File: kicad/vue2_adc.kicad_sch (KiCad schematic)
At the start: 141 parts, among them J1 AudioJack3_Ground, J10 AudioJack3_Ground, J11 AudioJack3_Ground, J12 AudioJack3_Ground, J13 AudioJack3_Ground, J14 AudioJack3_Ground, J15 AudioJack3_Ground, J16 AudioJack3_Ground, J18 AudioJack3_Ground, J19 AudioJack3_Ground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

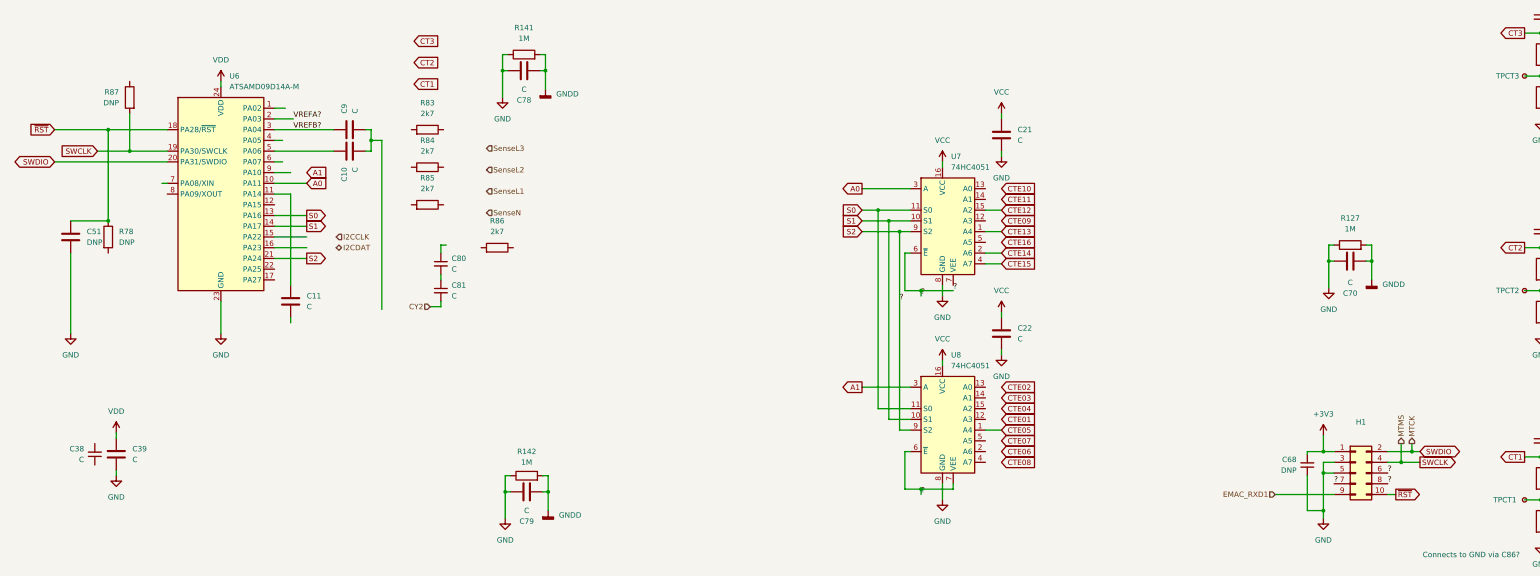
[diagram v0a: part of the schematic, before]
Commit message: Update schematic
As described in https://github.com/emporia-vue-local/esphome/discussions/173#discussioncomment-6137086

Thank you @g3gg0!

Also this ends up upgrading the project to Kicad 7
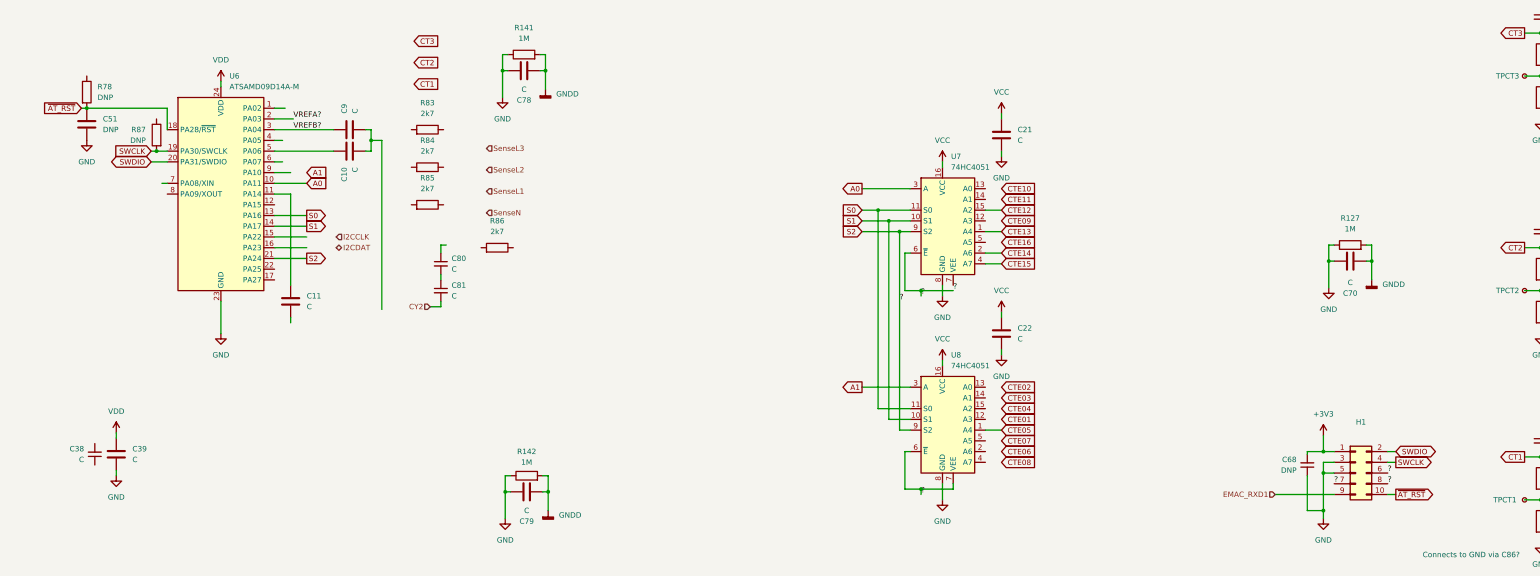
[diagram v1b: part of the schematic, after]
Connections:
- net ~{AT_RST}: now reaches R78.2
- net ~{AT_RST}: now also C51.1, H1.10 (Pin_10), U6.18 (PA28/~{RST})
- removed net ~{RST}: C51.1, H1.10 (Pin_10), R78.1, U6.18 (PA28/~{RST})
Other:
- moved on the sheet: C51, R78, R87
